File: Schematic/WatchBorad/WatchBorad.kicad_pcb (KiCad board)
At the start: 4 copper layers, 35 x 35 mm, 115 parts, among them J3 TYPE-C-31-M-17, M1 Motor_DC, SW1 SW_Push, SW2 SW_Push, SW3 SW_Push, SW4 SW_Push, SW5 SW_Push, U1 LSM6DSLTR, U10 M41T62Q6F, U11 GC9A01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

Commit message: Fixed capacitors near the fuel gauge [PCB]
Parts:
- moved C31 1.98 mm to (91.5, 98.2)
- moved C30 0.96 mm to (91.5, 99.8), turned to 0 degrees
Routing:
- net +BATT: track 43.3 -> 35.4 mm, vias 8 -> 9
- net GND: vias 74 -> 75

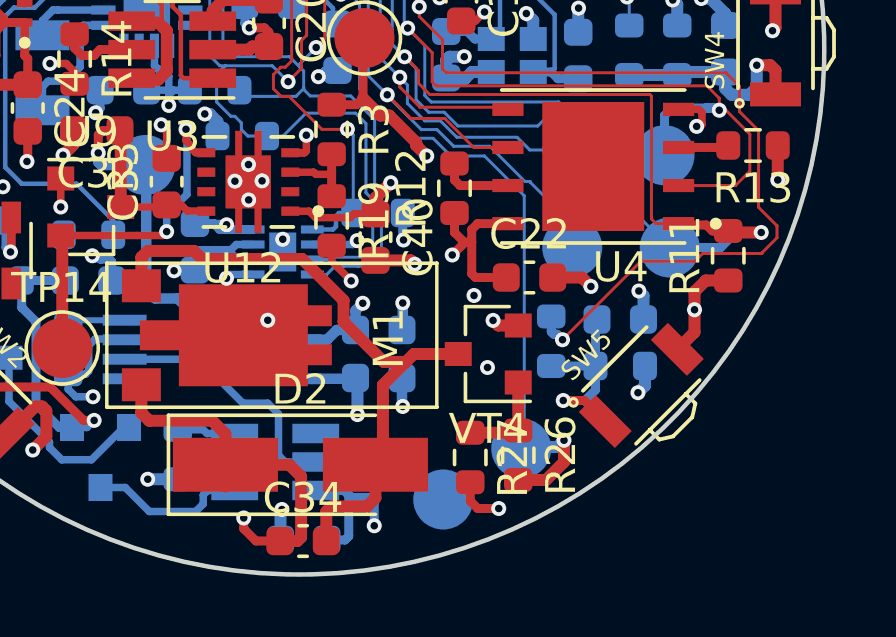
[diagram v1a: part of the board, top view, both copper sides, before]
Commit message: Added testpoint to the on/off circuit [PCB][SCHEMATIC]
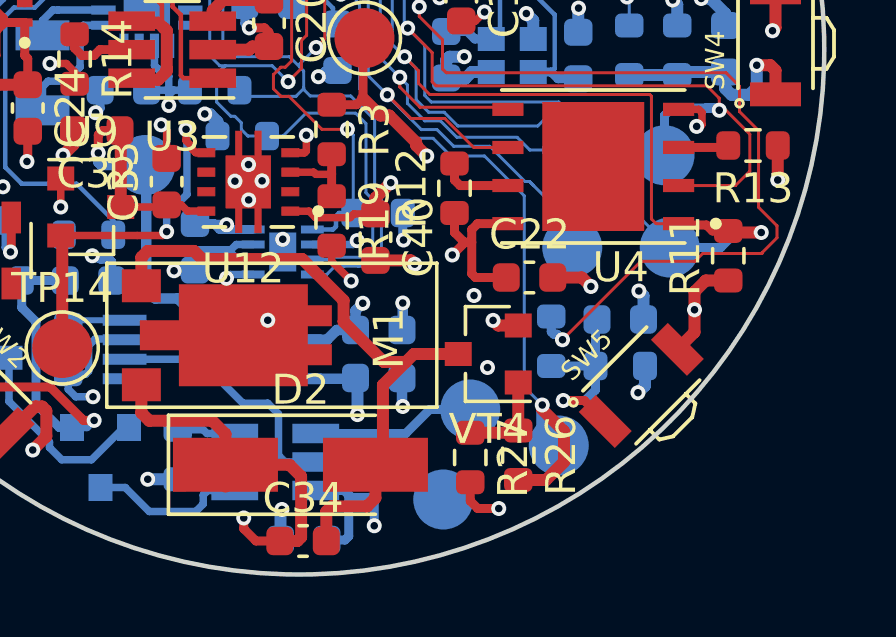
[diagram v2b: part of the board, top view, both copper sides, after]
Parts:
- added TP20: TestPoint, TestPoint:TestPoint_Pad_D2.0mm, B.Cu at (94.6, 100.9)
- R19: value 220 -> 220k
- R3: value 330 -> 330k
- moved TP13 1.25 mm to (97.5, 102.1)
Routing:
- net Net-(TP20-Pad1): track 0.00 -> 5.48 mm
- net /DCDC&PB/Enable_motor: track 23.5 -> 24.5 mm

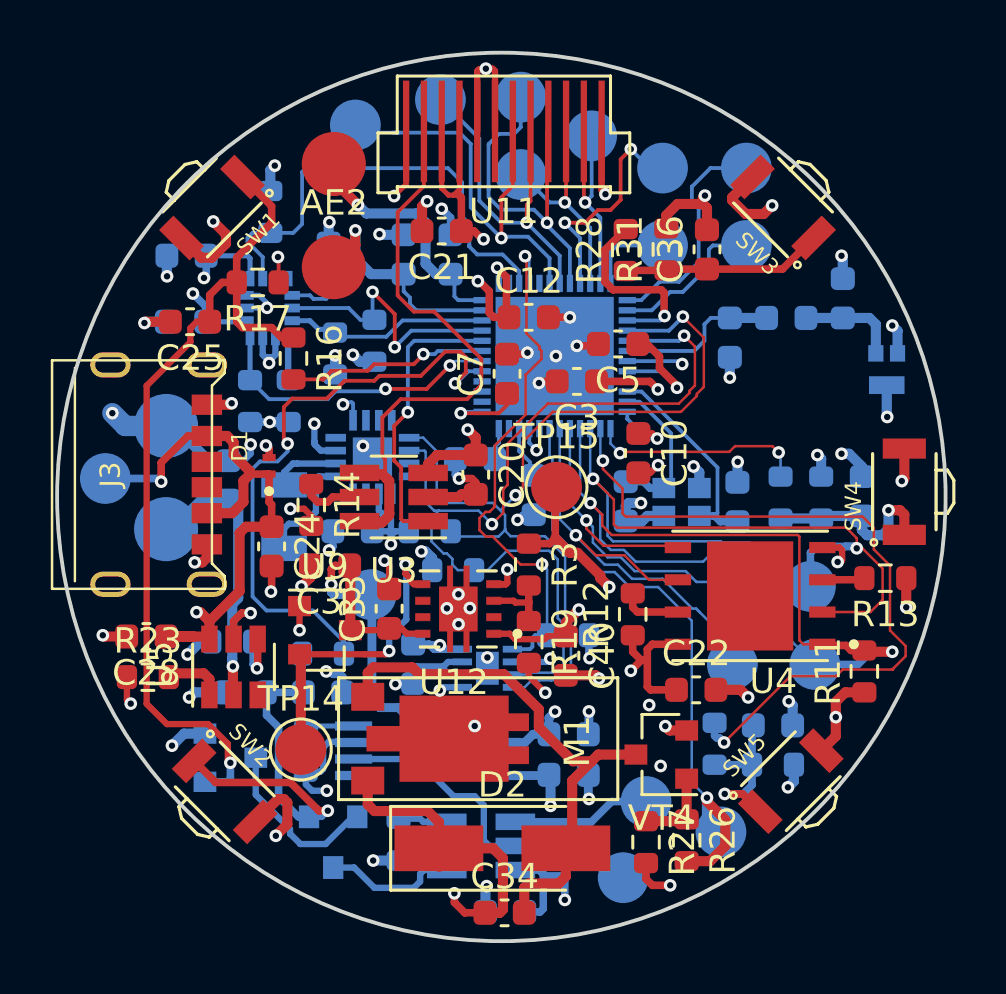
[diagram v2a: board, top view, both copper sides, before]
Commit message: Refactored routing near the LDO(capacitors + resistors) [PCB][SCHEMATIC]
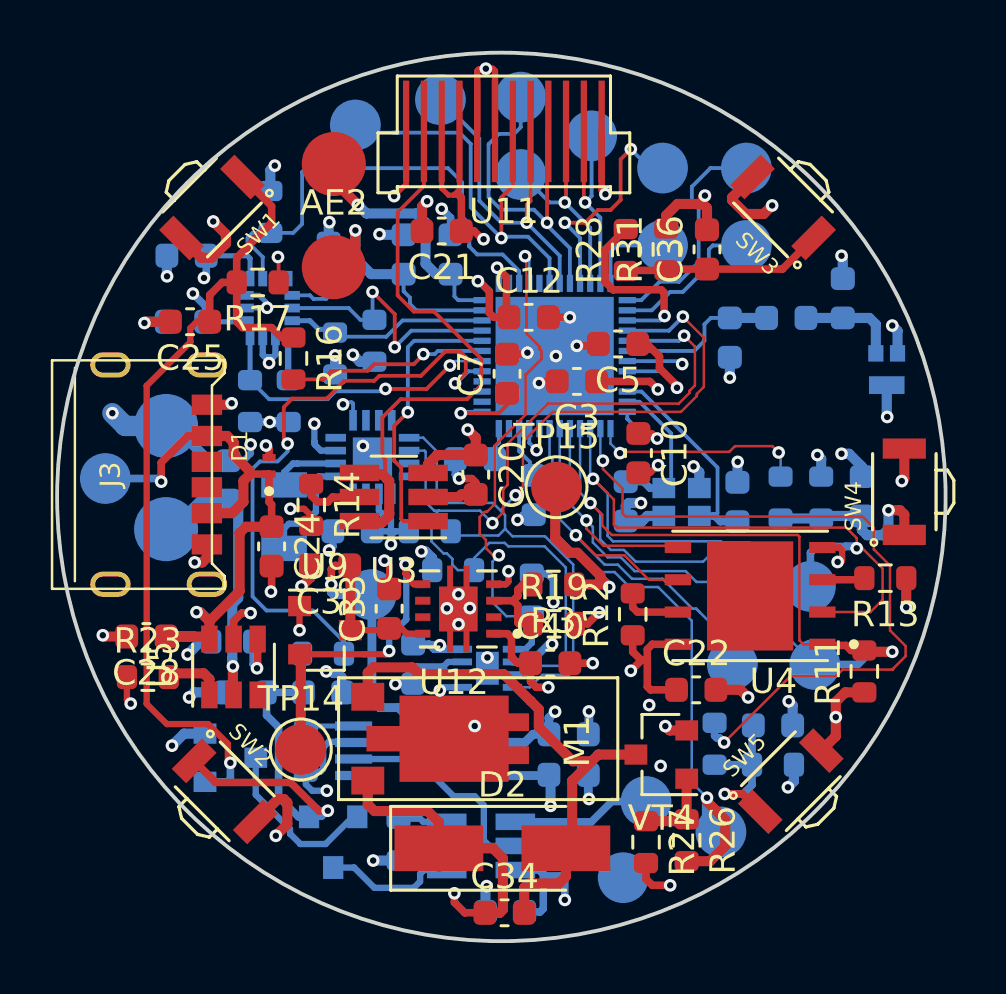
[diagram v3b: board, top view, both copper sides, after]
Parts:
- moved R10 2.14 mm to (90.1, 92.8), turned to 270 degrees
- moved R3 1.25 mm to (91.0, 92.3), turned to 180 degrees
- moved R19 1.23 mm to (91.0, 93.9), turned to 0 degrees
- moved C40 0.68 mm to (90.8, 95.5), turned to 0 degrees
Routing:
- net +3V3: track 76.9 -> 77.8 mm
- net /DCDC&PB/LDO_RDIV: track 2.77 -> 3.49 mm
- net /MCU/FG_OD_ALRT_N: track 21.0 -> 20.4 mm
- net /MCU/SCL_FG: track 35.7 -> 36.3 mm
- net GND: track 106.4 -> 105.9 mm

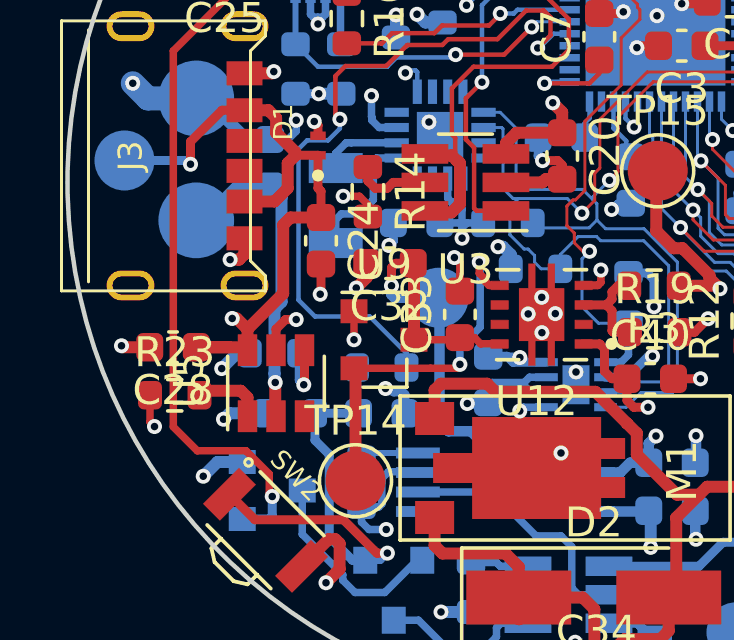
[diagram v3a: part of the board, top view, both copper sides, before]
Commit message: Removed away the trace between Battery input and the battery charger [PCB]
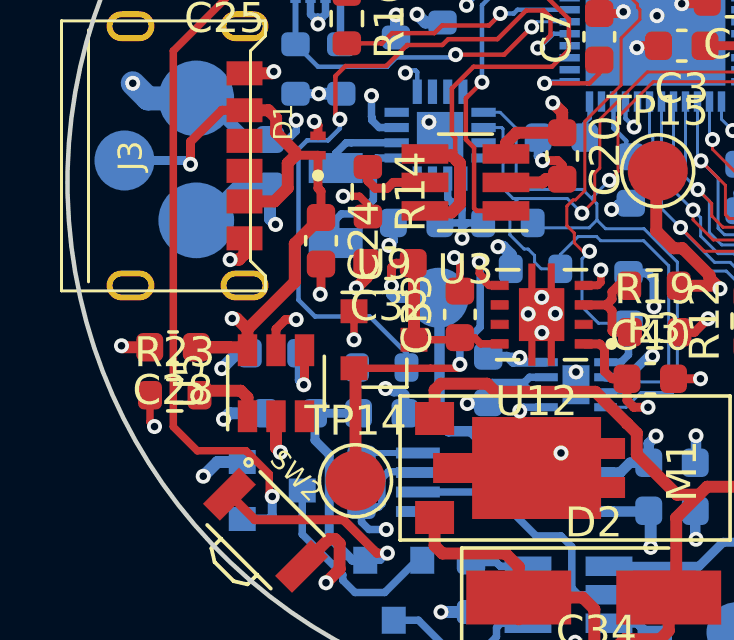
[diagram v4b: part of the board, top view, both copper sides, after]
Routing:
- net +BATT: track 35.4 -> 30.1 mm, vias 9 -> 10
- net +5V: track 26.6 -> 26.1 mm
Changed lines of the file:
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@@
     (thickness 1.6)
     (drawings 1)
-    (tracks 1342)
+    (tracks 1339)
     (zones 0)
     (modules 116)
@@
   )
   (setup
-    (last_trace_width 0.3)
+    (last_trace_width 0.4)
     (user_trace_width 0.1)
     (user_trace_width 0.15)
@@
   (via (at 76.89 93.44) (size 0.5) (drill 0.25) (layers F.Cu B.Cu) (net 3))
   (segment (start 77.43 94.47) (end 77.4 94.5) (width 0.4) (layer F.Cu) (net 3))
-  (segment (start 78.835 90.075) (end 79.85 90.075) (width 0.4) (layer F.Cu) (net 3))
-  (segment (start 78.59 90.32) (end 78.835 90.075) (width 0.4) (layer F.Cu) (net 3))
-  (segment (start 78.59 92.608667) (end 78.59 90.32) (width 0.4) (layer F.Cu) (net 3))
-  (segment (start 77.4 93.798667) (end 78.59 92.608667) (width 0.4) (layer F.Cu) (net 3))
   (segment (start 77.4 94.5) (end 77.4 93.798667) (width 0.4) (layer F.Cu) (net 3))
   (segment (start 77.041333 93.44) (end 77.4 93.798667) (width 0.4) (layer F.Cu) (net 3))
@@
   (segment (start 90.750001 99.874999) (end 90.775 99.85) (width 0.35) (layer B.Cu) (net 3))
   (segment (start 88.921 99.874999) (end 90.750001 99.874999) (width 0.35) (layer B.Cu) (net 3))
+  (segment (start 77.4 93.798667) (end 78.975395 92.223272) (width 0.4) (layer F.Cu) (net 3))
+  (segment (start 78.975395 92.223272) (end 78.975395 90.949605) (width 0.4) (layer F.Cu) (net 3))
+  (segment (start 78.975395 90.949605) (end 79.85 90.075) (width 0.4) (layer F.Cu) (net 3))
   (segment (start 100.9 81.85) (end 102.35 81.85) (width 0.4) (layer B.Cu) (net 4))
   (segment (start 103.4 81.85) (end 102.35 81.85) (width 0.4) (layer B.Cu) (net 4))
@@
   (segment (start 75.93 90.17) (end 77.075 89.025) (width 0.4) (layer B.Cu) (net 6))
   (segment (start 78.4 96.75) (end 78.35 96.7) (width 0.4) (layer F.Cu) (net 6))
-  (segment (start 78.534194 89.409194) (end 78.534194 92.889255) (width 0.4) (layer B.Cu) (net 6))
-  (segment (start 78.3 93.123449) (end 78.3 95.275004) (width 0.4) (layer B.Cu) (net 6))
-  (segment (start 78.534194 92.889255) (end 78.3 93.123449) (width 0.4) (layer B.Cu) (net 6))
-  (segment (start 78.15 89.025) (end 78.534194 89.409194) (width 0.4) (layer B.Cu) (net 6))
-  (via (at 78.325 95.575) (size 0.5) (drill 0.25) (layers F.Cu B.Cu) (net 6))
-  (segment (start 78.3 95.55) (end 78.325 95.575) (width 0.4) (layer B.Cu) (net 6))
-  (segment (start 78.3 95.275004) (end 78.3 95.55) (width 0.4) (layer B.Cu) (net 6))
   (segment (start 78.325 96.675) (end 78.35 96.7) (width 0.4) (layer F.Cu) (net 6))
-  (segment (start 78.325 95.575) (end 78.325 96.675) (width 0.4) (layer F.Cu) (net 6))
   (segment (start 90.4 103.6) (end 89.45 103.6) (width 0.3) (layer B.Cu) (net 6))
   (segment (start 90.55 103.75) (end 90.4 103.6) (width 0.3) (layer B.Cu) (net 6))
@@
   (segment (start 90.775 98.25) (end 90.775 97.601058) (width 0.35) (layer B.Cu) (net 6))
   (segment (start 90.775 97.601058) (end 91.01702 97.359038) (width 0.35) (layer B.Cu) (net 6))
+  (via (at 78.335394 90.306493) (size 0.5) (drill 0.25) (layers F.Cu B.Cu) (net 6))
+  (segment (start 78.15 90.121099) (end 78.335394 90.306493) (width 0.4) (layer B.Cu) (net 6))
+  (segment (start 78.15 89.025) (end 78.15 90.121099) (width 0.4) (layer B.Cu) (net 6))
+  (via (at 78.5 97.9) (size 0.5) (drill 0.25) (layers F.Cu B.Cu) (net 6))
+  (segment (start 78.35 97.75) (end 78.5 97.9) (width 0.4) (layer F.Cu) (net 6))
+  (segment (start 78.35 96.7) (end 78.35 97.75) (width 0.4) (layer F.Cu) (net 6))
   (segment (start 96.7 89.65) (end 97.3 89.65) (width 0.3) (layer B.Cu) (net 7))
   (segment (start 97.525 89.875) (end 98.2 89.875) (width 0.3) (layer B.Cu) (net 7))

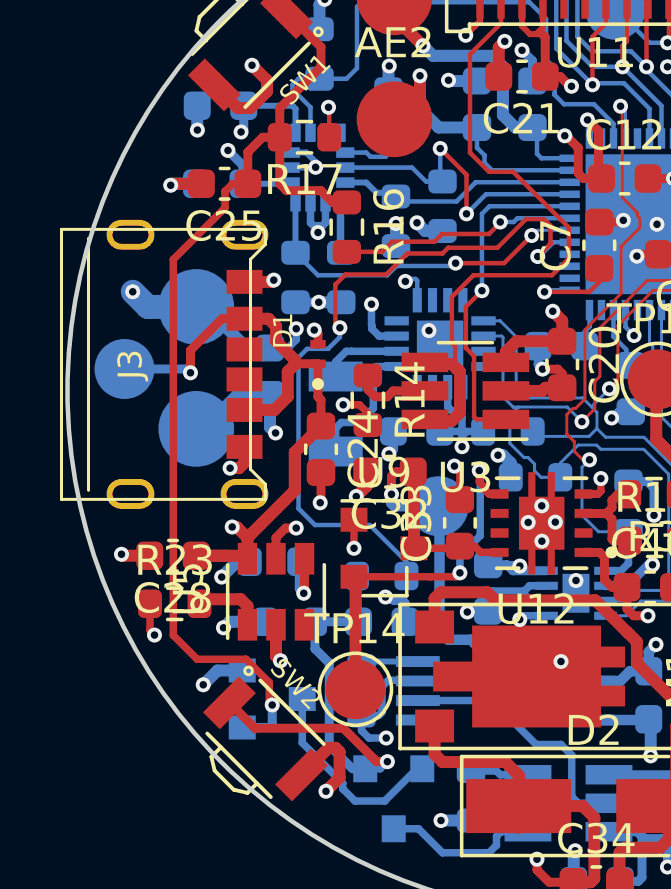
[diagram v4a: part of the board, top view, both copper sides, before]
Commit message: Fixed +5V traces. Moved them to the internal layer [PCB]
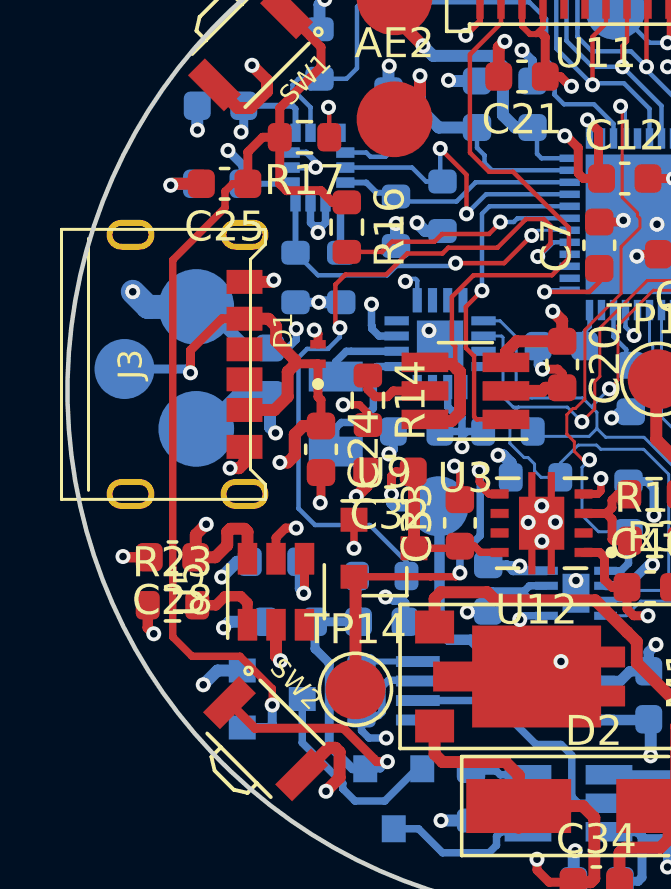
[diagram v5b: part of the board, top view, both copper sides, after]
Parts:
- moved R23 0.09 mm to (74.9, 96.0)
- moved C28 0.05 mm to (74.9, 94.5)
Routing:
- net +5V: track 26.1 -> 24.1 mm, vias 3 -> 4

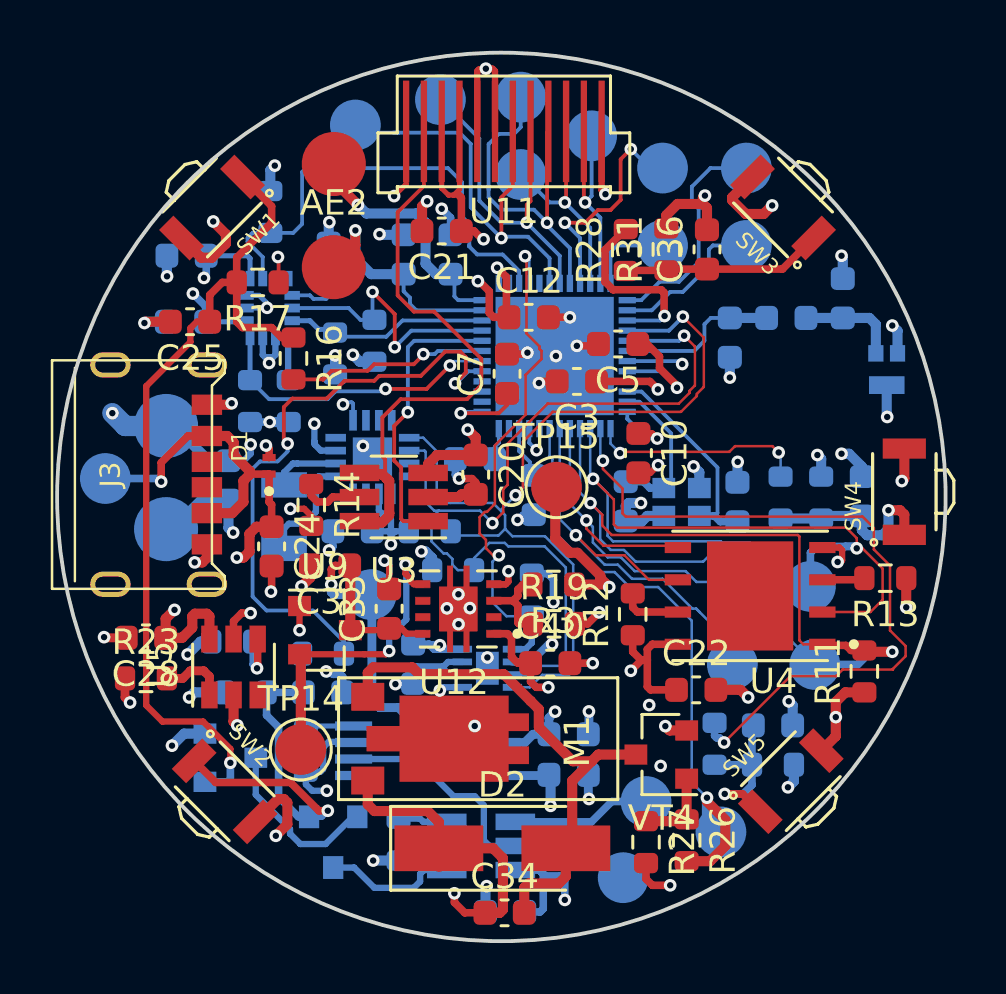
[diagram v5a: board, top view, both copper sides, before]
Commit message: Changed accelerometer to LSM6DSRTR [SCHEMATIC][PCB]
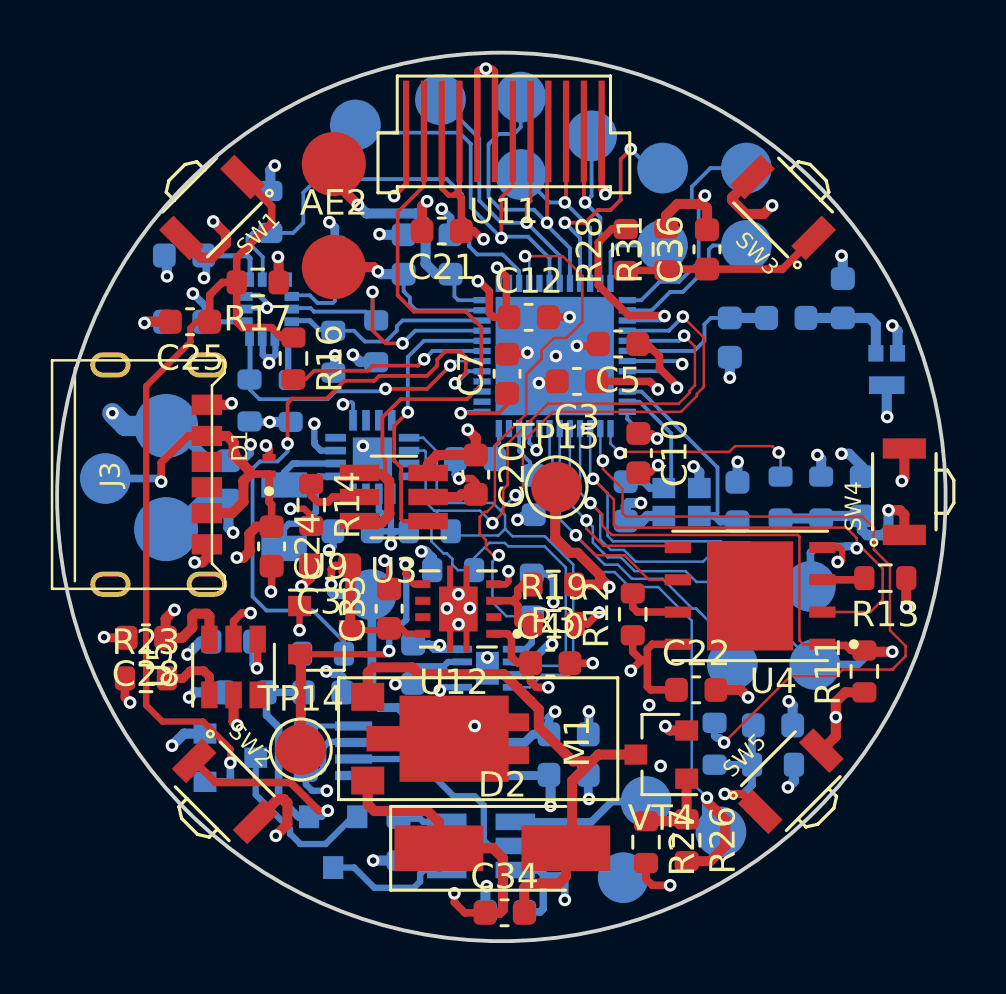
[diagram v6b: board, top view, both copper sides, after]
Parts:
- U1: value LSM6DSLTR -> LSM6DSRTR; footprint LocalFootprints:LSM6DSLTR -> LSM6DSRTR:LSM6DSRTR_LGA-14L
- moved R8 6.26 mm to (79.0, 85.1), turned to 90 degrees
- moved R5 4.17 mm to (84.0, 82.8)
- moved R7 4.06 mm to (80.6, 85.1)
- moved R4 3.81 mm to (82.3, 83.2)
- moved R6 3.42 mm to (82.3, 79.8), turned to 270 degrees
- moved C14 0.10 mm to (76.4, 79.4)
- moved C16 0.07 mm to (76.4, 82.0)
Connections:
- J3 pad A5: Net-(J3-PadA5) -> (no net)
- J3 pad B5: Net-(J3-PadB5) -> (no net)
- R4 pad 2: /MCU/MPU_INT_1 -> /MCU/I2C_SDA
- R5 pad 2: Net-(R5-Pad2) -> /MCU/I2C_SCL
- R6 pad 2: /MCU/I2C_SDA -> /MCU/NC_PU
- R7 pad 2: /MCU/I2C_SCL -> Net-(R7-Pad2)
- R8 pad 2: /MCU/NC_PU -> /MCU/MPU_INT_1
- U1 pad 1: Net-(R5-Pad2) -> Net-(R7-Pad2)
- U1 pad 10: Net-(U1-Pad10) -> (no net)
- U1 pad 11: Net-(U1-Pad11) -> (no net)
- U10 pad 11: Net-(U10-Pad11) -> (no net)
- U10 pad 12: Net-(U10-Pad12) -> (no net)
- U10 pad 13: Net-(U10-Pad13) -> (no net)
- U10 pad 15: Net-(U10-Pad15) -> (no net)
- U10 pad 16: Net-(U10-Pad16) -> (no net)
- U10 pad 4: Net-(U10-Pad4) -> (no net)
- U10 pad 6: Net-(U10-Pad6) -> (no net)
- U10 pad 7: Net-(U10-Pad7) -> (no net)
- U10 pad 8: Net-(U10-Pad8) -> (no net)
- U2 pad 14: /MCU/P5 -> (no net)
- U2 pad 17: /MCU/P17 -> (no net)
- U2 pad 2: /MCU/XL1 -> (no net)
- U2 pad 3: /MCU/XL2 -> (no net)
- U2 pad 4: /MCU/P6 -> (no net)
- U2 pad 44: Net-(U2-Pad44) -> (no net)
- U2 pad 47: Net-(U2-Pad47) -> (no net)
- U5 pad 3: Net-(U5-Pad3) -> (no net)
- U8 pad 1: Net-(U8-Pad1) -> (no net)
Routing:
- net /MCU/FG_OD_ALRT_N: track 20.4 -> 22.9 mm
- net /MCU/NFC1: track 9.28 -> 7.09 mm
- net Net-(R7-Pad2): track 0.00 -> 1.69 mm
- net Net-(R5-Pad2): track 1.69 -> 0.00 mm
- net /MCU/MPU_INT_2: track 19.2 -> 18.0 mm
- net /MCU/LEDK: track 23.5 -> 24.2 mm
- net /MCU/NC_PU: track 2.04 -> 2.76 mm
- net +3V3: track 77.8 -> 78.4 mm
- net /MCU/I2C_SDA: track 8.32 -> 8.91 mm
